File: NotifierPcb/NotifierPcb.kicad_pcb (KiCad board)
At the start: 2 copper layers, 81.6 x 97.9 mm, 30 parts, among them IC1 CD4067BEE4, IC2 ESP32-WROOM-32E__8MB_, J1 RC_433_MHZ_RF, J2 UART_Conn, J3 Power_Conn, J4 Vcc, J5 Vcc, J6 Vcc, U1 HT75xx-1-SOT89

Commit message: make pads bigger
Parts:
- J6: footprint Connector_PinHeader_1.00mm:PinHeader_1x02_P1.00mm_Vertical -> Connector_PinHeader_2.54mm:PinHeader_1x02_P2.54mm_Vertical
- moved J6 0.35 mm to (136.5, 77.5)
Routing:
- net +3.3V: track 220.8 -> 212.5 mm

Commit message: new configuratio for boot pins selection
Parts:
- removed J4: Vcc, Connector_PinHeader_1.00mm:PinHeader_1x01_P1.00mm_Vertical
- removed R1: 10kΩ, Resistor_THT:R_Axial_DIN0204_L3.6mm_D1.6mm_P2.54mm_Vertical
- added J5: Vcc, Connector_PinHeader_1.00mm:PinHeader_1x01_P1.00mm_Vertical, F.Cu at (173.0, 66.0)
- added JP2: Boot_Jumper_Flash, Connector_PinHeader_2.54mm:PinHeader_1x02_P2.54mm_Vertical, F.Cu at (170.3, 61.3)
- added JP3: Boot_Jumper_Download, Connector_PinHeader_2.54mm:PinHeader_1x02_P2.54mm_Vertical, F.Cu at (170.3, 61.3)
- added JP4: Enable_Jumper, Connector_PinHeader_2.54mm:PinHeader_1x02_P2.54mm_Vertical, F.Cu at (120.8, 63.7)
- JP1: value Boot_Jumper -> Enable_Jumper
- moved JP1 39.9 mm to (120.8, 63.7), turned to 0 degrees
- moved J2 14.4 mm to (173.9, 49.4), turned to -90 degrees
- moved IC1 1.75 mm to (142.2, 97.0)
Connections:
- IC2 pad 24: BOOT -> GND
- JP1 pad 1: GND -> ESP32_EN
- JP1 pad 2: BOOT -> +3.3V
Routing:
- net +3.3V: track 212.5 -> 258.5 mm
- net ESP32_EN: track 0.00 -> 22.5 mm
- net UART_RX: track 22.7 -> 32.4 mm
- net BOOT: track 16.0 -> 22.4 mm
- net BIT3: track 13.4 -> 19.3 mm
- net BIT2: track 16.1 -> 21.8 mm
- net GND: track 233.1 -> 228.0 mm
- net LED7: track 31.2 -> 26.5 mm
- net UART_TX: track 26.4 -> 30.9 mm
- net LED12: track 30.9 -> 26.8 mm
- net LED11: track 31.6 -> 27.5 mm
- net LED15: track 27.8 -> 25.1 mm
- net LED14: track 30.2 -> 27.5 mm
- net LED13: track 30.8 -> 28.0 mm
- net LED9: track 28.7 -> 26.1 mm
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- removed copper zone on F.Cu, net GND

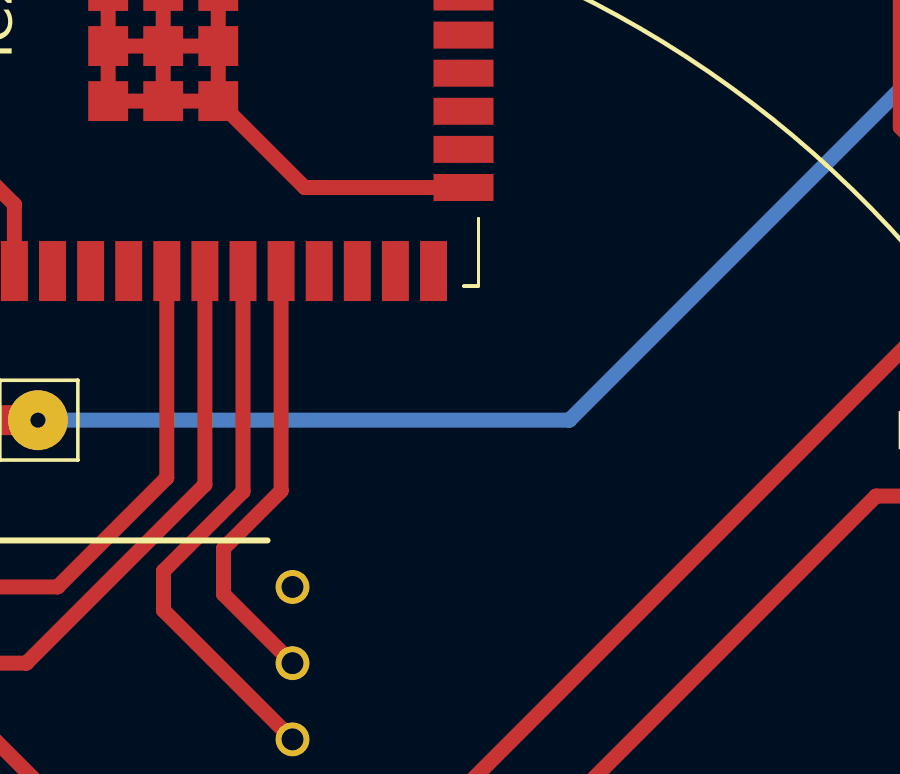
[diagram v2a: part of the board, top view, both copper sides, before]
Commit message: add gnd for cd4067
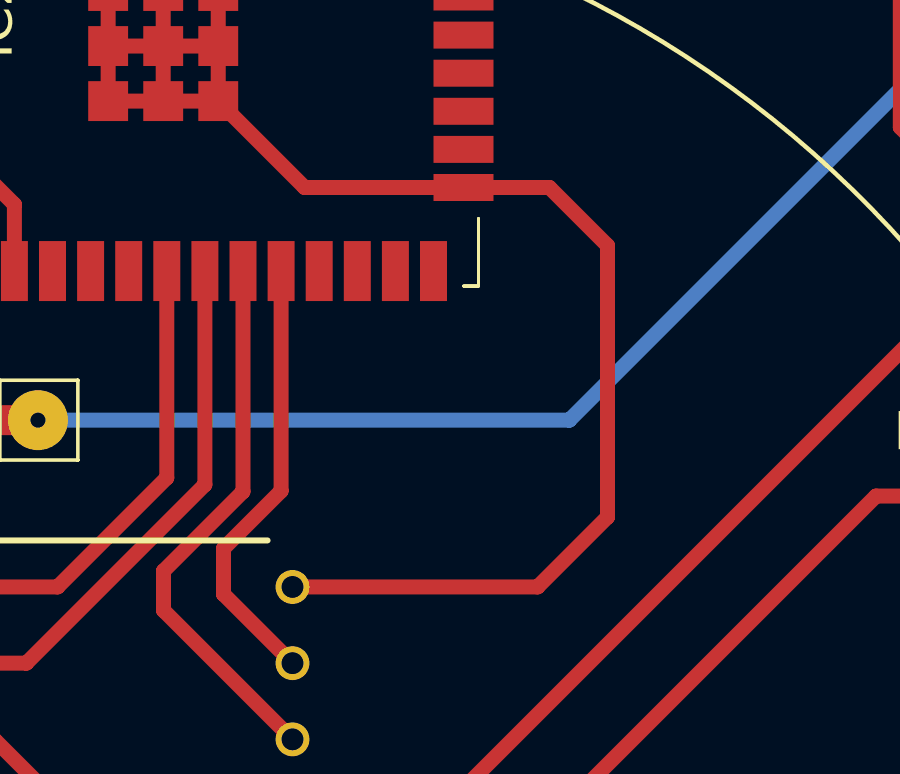
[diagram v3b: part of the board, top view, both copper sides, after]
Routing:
- net GND: track 228.0 -> 254.1 mm
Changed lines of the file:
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@@
   (segment (start 159.535 58.285) (end 162.55 61.3) (width 0.5) (layer "F.Cu") (net 12))
   (segment (start 141.405 66.835) (end 145.075 66.835) (width 0.5) (layer "F.Cu") (net 12))
+  (segment (start 158.05 71.65) (end 158.05 80.7) (width 0.5) (layer "F.Cu") (net 12))
   (segment (start 143.0665 116.9165) (end 144.75 118.6) (width 0.5) (layer "F.Cu") (net 12))
+  (segment (start 155.72 83.03) (end 147.55 83.03) (width 0.5) (layer "F.Cu") (net 12))
   (segment (start 132.45 88.11) (end 137.61 88.11) (width 0.5) (layer "F.Cu") (net 12))
+  (segment (start 156.115 69.715) (end 158.05 71.65) (width 0.5) (layer "F.Cu") (net 12))
   (segment (start 103.775 57.275) (end 110.152651 57.275) (width 0.5) (layer "F.Cu") (net 12))
+  (segment (start 158.05 80.7) (end 155.72 83.03) (width 0.5) (layer "F.Cu") (net 12))
   (segment (start 147.955 69.715) (end 153.25 69.715) (width 0.5) (layer "F.Cu") (net 12))
   (segment (start 145.075 62.175) (end 145.075 63.165) (width 0.5) (layer "F.Cu") (net 12))
@@
   (segment (start 143.0665 123.7335) (end 142.85 123.95) (width 1) (layer "F.Cu") (net 12))
   (segment (start 145.075 66.835) (end 147.955 69.715) (width 0.5) (layer "F.Cu") (net 12))
+  (segment (start 153.25 69.715) (end 156.115 69.715) (width 0.5) (layer "F.Cu") (net 12))
   (segment (start 137.61 88.11) (end 143 93.5) (width 0.5) (layer "F.Cu") (net 12))
   (segment (start 141.405 63.165) (end 145.075 63.165) (width 0.5) (layer "F.Cu") (net 12))
